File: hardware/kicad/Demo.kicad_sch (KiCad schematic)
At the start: 7 parts, among them J701 Conn_01x06_Pin, J702 Conn_01x06_Pin, J703 Conn_01x06_Pin, J704 Conn_01x06_Pin

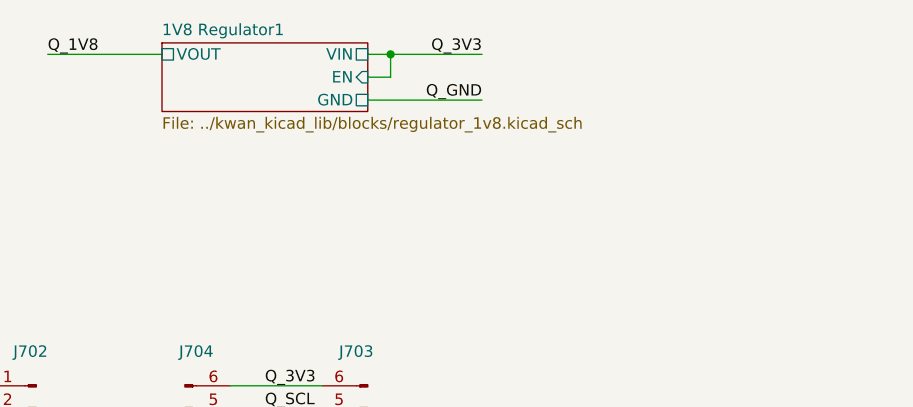
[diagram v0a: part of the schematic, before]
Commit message: Imported shipometer hat 23.04 as built, updated to Kicad 9
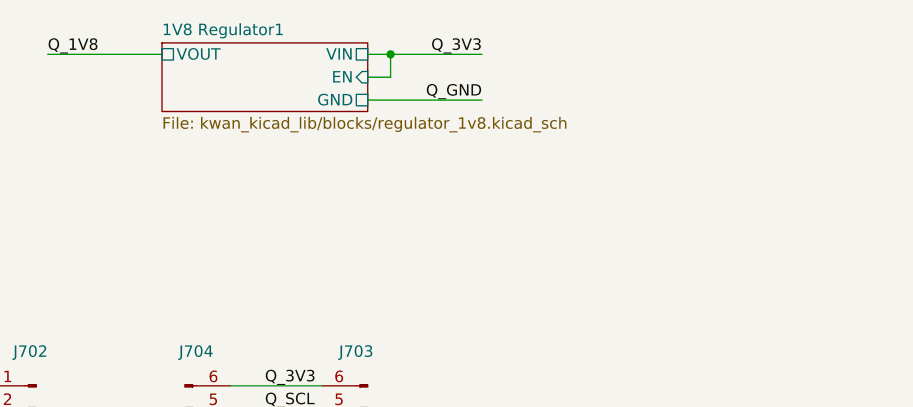
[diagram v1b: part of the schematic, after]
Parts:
- renumbered G1 to G701, G2 to G702, G3 to G703
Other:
- sheet 1V8 Regulator1: file ../kwan_kicad_lib/blocks/regulator_1v8.kicad_sch -> kwan_kicad_lib/blocks/regulator_1v8.kicad_sch
